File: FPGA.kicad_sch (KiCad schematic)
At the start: 8 parts, among them U4 GW1N_LV4QN32C6/I5

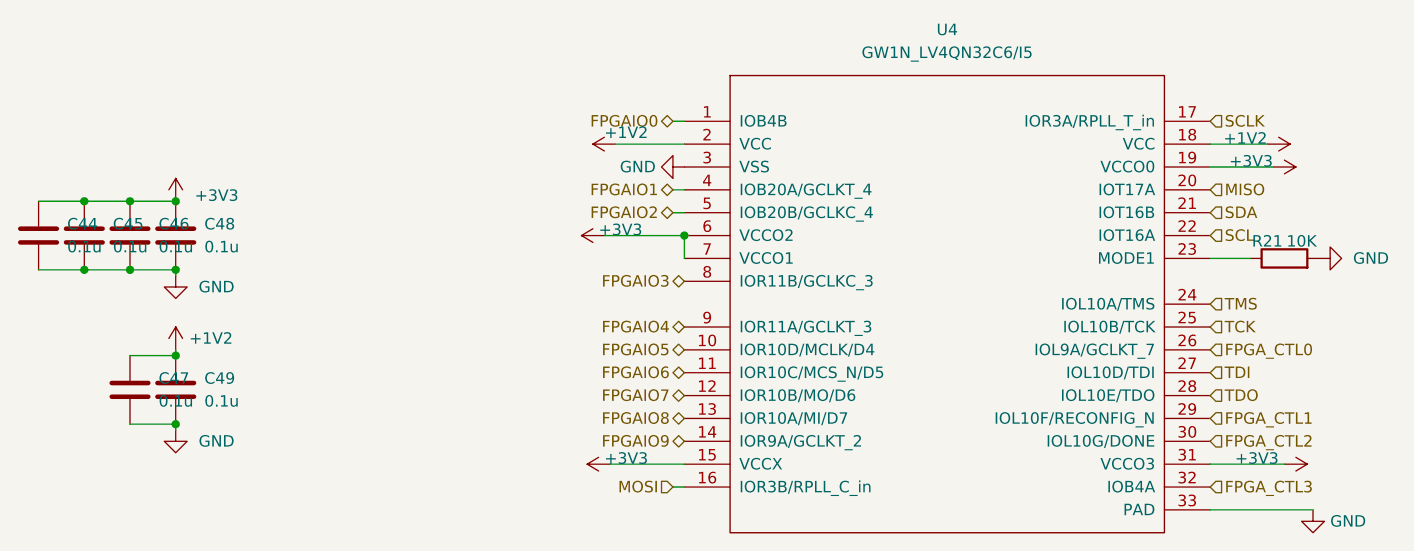
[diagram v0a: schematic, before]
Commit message: use LDO to produce 1.2V, to fix fpga voltage issue. fix wrong fpga sch issue, change the pins of fpga. connect fpga SSPI to V3s-spi, so that we can configuare fpag on v3s someday.
Signed-off-by: ncerzzk <huangzzk@bupt.edu.cn>
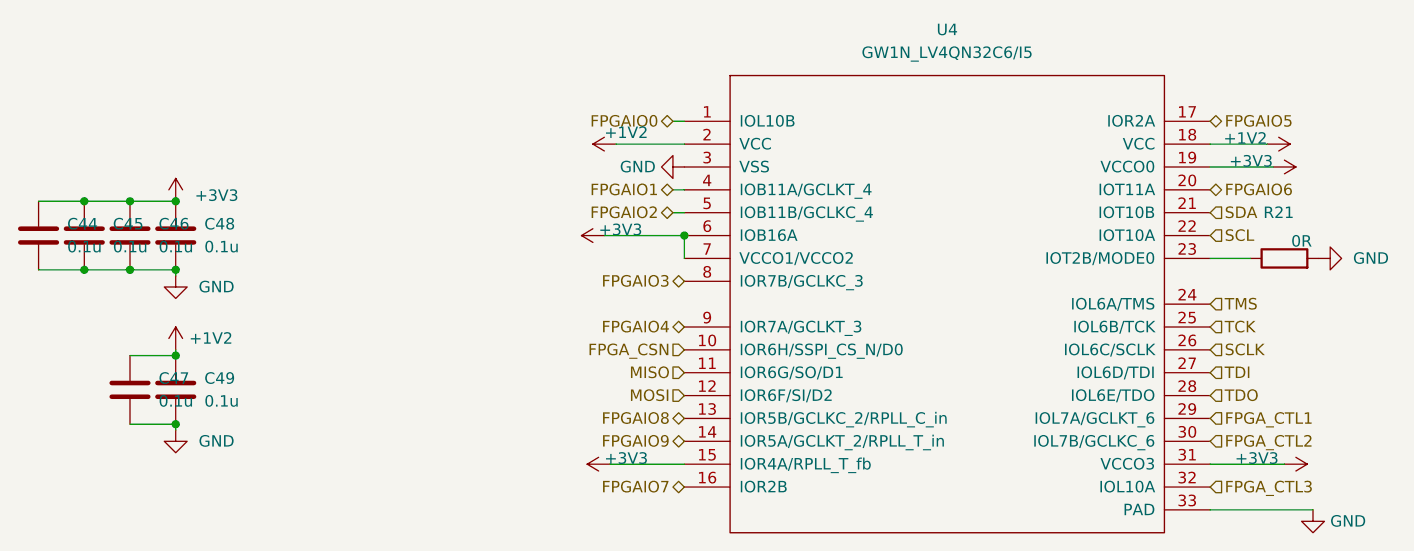
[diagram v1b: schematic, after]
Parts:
- R21: value 10K -> 0R
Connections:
- net FPGA_CTL0 is gone; now on net SCLK: U4.26 (IOL6C/SCLK)
- net FPGAIO5: now also U4.17 (IOR2A); no longer U4.10 (IOR10D/MCLK/D4)
- net FPGAIO6: now also U4.20 (IOT11A); no longer U4.11 (IOR10C/MCS_N/D5)
- net FPGAIO7: now also U4.16 (IOR2B); no longer U4.12 (IOR10B/MO/D6)
- net MISO: now also U4.11 (IOR6G/SO/D1); no longer U4.20 (IOT17A)
- net MOSI: now also U4.12 (IOR6F/SI/D2); no longer U4.16 (IOR3B/RPLL_C_in)
- net SCLK: no longer U4.17 (IOR3A/RPLL_T_in)
- new net FPGA_CSN: U4.10 (IOR6H/SSPI_CS_N/D0)
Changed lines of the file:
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@@
-    (stroke (width 0) (type default) (color 0 0 0 0))
-  )
-  (wire (pts (xy 94.615 97.155) (xy 95.885 97.155))
     (stroke (width 0) (type default) (color 0 0 0 0))
   )
@@
     (effects (font (size 1.27 1.27)) (justify right))
   )
+  (hierarchical_label "FPGAIO6" (shape bidirectional) (at 154.305 64.135 0)
+    (effects (font (size 1.27 1.27)) (justify left))
+  )
   (hierarchical_label "FPGAIO2" (shape bidirectional) (at 94.615 66.675 180)
     (effects (font (size 1.27 1.27)) (justify right))
@@
     (effects (font (size 1.27 1.27)) (justify left))
   )
+  (hierarchical_label "FPGAIO7" (shape bidirectional) (at 95.885 97.155 180)
+    (effects (font (size 1.27 1.27)) (justify right))
+  )
   (hierarchical_label "FPGAIO8" (shape bidirectional) (at 95.885 89.535 180)
     (effects (font (size 1.27 1.27)) (justify right))
   )
-  (hierarchical_label "FPGAIO7" (shape bidirectional) (at 95.885 86.995 180)
-    (effects (font (size 1.27 1.27)) (justify right))
-  )
   (hierarchical_label "FPGAIO1" (shape bidirectional) (at 94.615 64.135 180)
     (effects (font (size 1.27 1.27)) (justify right))
   )
-  (hierarchical_label "MOSI" (shape input) (at 94.615 97.155 180)
-    (effects (font (size 1.27 1.27)) (justify right))
-  )
-  (hierarchical_label "MISO" (shape input) (at 154.305 64.135 0)
-    (effects (font (size 1.27 1.27)) (justify left))
+  (hierarchical_label "MISO" (shape input) (at 95.885 84.455 180)
+    (effects (font (size 1.27 1.27)) (justify right))
+  )
+  (hierarchical_label "MOSI" (shape input) (at 95.885 86.995 180)
+    (effects (font (size 1.27 1.27)) (justify right))
   )
   (hierarchical_label "FPGAIO3" (shape bidirectional) (at 95.885 74.295 180)
     (effects (font (size 1.27 1.27)) (justify right))
   )
+  (hierarchical_label "SCLK" (shape input) (at 154.305 81.915 0)
+    (effects (font (size 1.27 1.27)) (justify left))
+  )
   (hierarchical_label "FPGAIO0" (shape bidirectional) (at 94.615 56.515 180)
     (effects (font (size 1.27 1.27)) (justify right))
@@
     (effects (font (size 1.27 1.27)) (justify left))
   )
-  (hierarchical_label "SCLK" (shape input) (at 154.305 56.515 0)
-    (effects (font (size 1.27 1.27)) (justify left))
-  )
-  (hierarchical_label "FPGA_CTL0" (shape input) (at 154.305 81.915 0)
-    (effects (font (size 1.27 1.27)) (justify left))
+  (hierarchical_label "FPGA_CSN" (shape input) (at 95.885 81.915 180)
+    (effects (font (size 1.27 1.27)) (justify right))
   )
   (hierarchical_label "FPGA_CTL3" (shape input) (at 154.305 97.155 0)
@@
     (effects (font (size 1.27 1.27)) (justify left))
   )
+  (hierarchical_label "FPGAIO5" (shape bidirectional) (at 154.305 56.515 0)
+    (effects (font (size 1.27 1.27)) (justify left))
+  )
   (hierarchical_label "FPGAIO9" (shape bidirectional) (at 95.885 92.075 180)
     (effects (font (size 1.27 1.27)) (justify right))
@@
   (hierarchical_label "TDI" (shape input) (at 154.305 84.455 0)
     (effects (font (size 1.27 1.27)) (justify left))
-  )
-  (hierarchical_label "FPGAIO6" (shape bidirectional) (at 95.885 84.455 180)
-    (effects (font (size 1.27 1.27)) (justify right))
-  )
-  (hierarchical_label "FPGAIO5" (shape bidirectional) (at 95.885 81.915 180)
-    (effects (font (size 1.27 1.27)) (justify right))
   )
   (symbol (lib_id "power:+3V3") (at 87.63 94.615 90) (unit 1)
@@
   (symbol (lib_id "Device:R") (at 162.56 71.755 90) (unit 1)
     (in_bom yes) (on_board yes)
-    (property "Reference" "R21" (id 0) (at 160.655 69.85 90))
-    (property "Value" "10K" (id 1) (at 164.465 69.85 90))
+    (property "Reference" "R21" (id 0) (at 161.925 66.675 90))
+    (property "Value" "0R" (id 1) (at 164.465 69.85 90))
     (property "Footprint" "Resistor_SMD:R_0402_1005Metric" (id 2) (at 162.56 73.533 90)
       (effects (font (size 1.27 1.27)) hide)

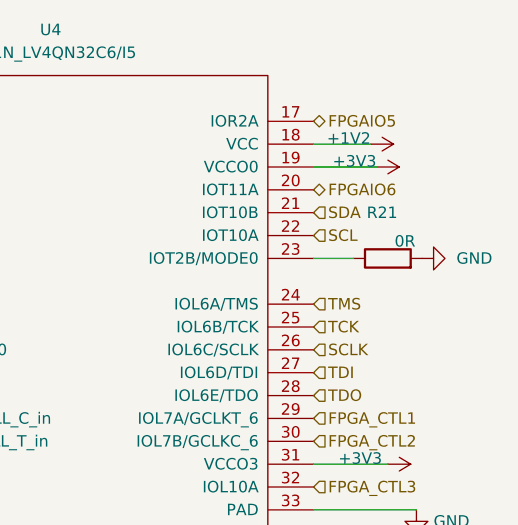
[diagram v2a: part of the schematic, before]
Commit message: add esp32 as wifi card
Signed-off-by: huangzzk <huangcmzzk@gmail.com>
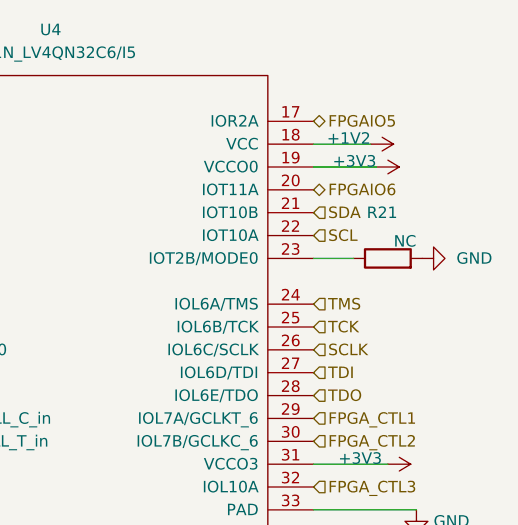
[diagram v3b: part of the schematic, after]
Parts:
- R21: value 0R -> NC
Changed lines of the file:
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@@
     (in_bom yes) (on_board yes)
     (property "Reference" "R21" (id 0) (at 161.925 66.675 90))
-    (property "Value" "0R" (id 1) (at 164.465 69.85 90))
+    (property "Value" "NC" (id 1) (at 164.465 69.85 90))
     (property "Footprint" "Resistor_SMD:R_0402_1005Metric" (id 2) (at 162.56 73.533 90)
       (effects (font (size 1.27 1.27)) hide)
